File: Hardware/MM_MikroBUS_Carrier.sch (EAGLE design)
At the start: 50 parts, among them J15 MICROMOD-2222-C, J2 QWIIC_RIGHT_ANGLE, J5 Vertical Qwiic Connector, U1 MCP73831, U5 AP7361C-33FGEUDFN-8

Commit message: Working on proto
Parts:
- added U3: MIKROBUS_SMD_BLACK1, mikroBUS_SMD_BLACK:MIKROBUS_SMD_BLACK1
- H5: value STAND-OFF-REFLOW2.5MM_TALL -> STAND-OFF-REFLOW-M2.5_2.5MM_TALL; device SparkFun-Hardware:STAND-OFF-REFLOW2.5MM_TALL -> SparkFun-Hardware:STAND-OFF-REFLOW-M2.5_2.5MM_TALL
- renumbered U5 to U2
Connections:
- removed net D0: J15.D0, J6.4
- removed net D1: J15.D1/CAM_TRIG, J6.5
- new net 5V: U3.+5V
- new net AN_IN: J15.A0, U3.AN
- new net MIK_INT: J15.D0, U3.INT
- new net MIK_RST: J15.D1/CAM_TRIG, U3.RST
- new net PWM: J15.PWM0, U3.PWM
- new net RX: J15.TX1, U3.RX
- new net TX: J15.RX1, U3.TX
- net 3.3V: now also U3.+3.3V
- net GND: now also U3.GND, U3.GND2
- net SCL: now also U3.SCL
- net SDA: now also U3.SDA
- net SPI_!CS!: now also U3.CS
- net SPI_CIPO: now also U3.CIPO
- net SPI_COPI: now also U3.COPI
- net SPI_SCK: now also U3.SCK
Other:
- note added: "MM-MikroBUS-Carrier"
- note added: "MikroBUS Socket"
- note added: "v01"
- note removed: "MM-Qwiic-Carrier-Single"
- note removed: "v10"

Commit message: Finished proto design
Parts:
- removed TP1, TP2: TEST-POINT3X5, SparkFun-Connectors:TEST-POINT3X5
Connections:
- net MIK_INT: now also J6.5
- net MIK_RST: now also J6.4
- net SCL: no longer TP2.1
- net SDA: no longer TP1.1
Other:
- note removed: "Test Points"
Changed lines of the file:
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@@
 <part name="SUPPLY8" library="SparkFun-PowerSymbols" deviceset="VIN" device=""/>
 <part name="SUPPLY9" library="SparkFun-PowerSymbols" deviceset="VIN" device=""/>
-<part name="TP1" library="SparkFun-Connectors" deviceset="TEST-POINT" device="3X5"/>
-<part name="TP2" library="SparkFun-Connectors" deviceset="TEST-POINT" device="3X5"/>
 <part name="J4" library="SparkFun-Connectors" deviceset="CONN_02" device="1X02_NO_SILK"/>
 <part name="GND14" library="SparkFun-PowerSymbols" deviceset="GND" device=""/>
@@
 <wire x1="330.2" y1="132.08" x2="431.8" y2="132.08" width="0.2032" layer="97" style="longdash"/>
 <text x="381" y="182.88" size="2.54" layer="94" font="vector" align="center">Power Source Select</text>
-<text x="381" y="121.92" size="2.54" layer="94" font="vector" align="center">Test Points</text>
 <text x="109.22" y="25.4" size="1.778" layer="97" font="vector">Qwiic bus conservative
 max current: 226mA</text>
@@
 <instance part="SUPPLY9" gate="G$1" x="22.86" y="236.22" smashed="yes">
 <attribute name="VALUE" x="22.86" y="239.014" size="1.778" layer="96" align="bottom-center"/>
-</instance>
-<instance part="TP1" gate="G$1" x="378.46" y="109.22" smashed="yes">
-<attribute name="NAME" x="375.92" y="111.76" size="1.778" layer="95" font="vector"/>
-</instance>
-<instance part="TP2" gate="G$1" x="378.46" y="99.06" smashed="yes">
-<attribute name="NAME" x="375.92" y="101.6" size="1.778" layer="95" font="vector"/>
 </instance>
 <instance part="J4" gate="G$1" x="307.34" y="139.7" smashed="yes" rot="R180">
@@
 <net name="SDA" class="0">
 <segment>
-<pinref part="TP1" gate="G$1" pin="1"/>
-<wire x1="378.46" y1="109.22" x2="375.92" y2="109.22" width="0.1524" layer="91"/>
-<label x="375.92" y="109.22" size="1.27" layer="95" rot="R180" xref="yes"/>
-</segment>
-<segment>
 <pinref part="J5" gate="G$1" pin="3"/>
 <wire x1="121.92" y1="48.26" x2="127" y2="48.26" width="0.1524" layer="91"/>
@@
 </net>
 <net name="SCL" class="0">
-<segment>
-<pinref part="TP2" gate="G$1" pin="1"/>
-<wire x1="378.46" y1="99.06" x2="375.92" y2="99.06" width="0.1524" layer="91"/>
-<label x="375.92" y="99.06" size="1.27" layer="95" rot="R180" xref="yes"/>
-</segment>
 <segment>
 <pinref part="J5" gate="G$1" pin="4"/>
@@
 <label x="86.36" y="208.28" size="1.27" layer="95" xref="yes"/>
 </segment>
+<segment>
+<pinref part="J6" gate="J1" pin="4"/>
+<wire x1="205.74" y1="20.32" x2="210.82" y2="20.32" width="0.1524" layer="91"/>
+<label x="210.82" y="20.32" size="1.27" layer="95" xref="yes"/>
+</segment>
 </net>
 <net name="AN_IN" class="0">
@@
 <label x="86.36" y="210.82" size="1.27" layer="95" xref="yes"/>
 </segment>
-</net>
+<segment>
+<pinref part="J6" gate="J1" pin="5"/>
+<wire x1="205.74" y1="22.86" x2="210.82" y2="22.86" width="0.1524" layer="91"/>
+<label x="210.82" y="22.86" size="1.27" layer="95" xref="yes"/>
+</segment>
+</net>

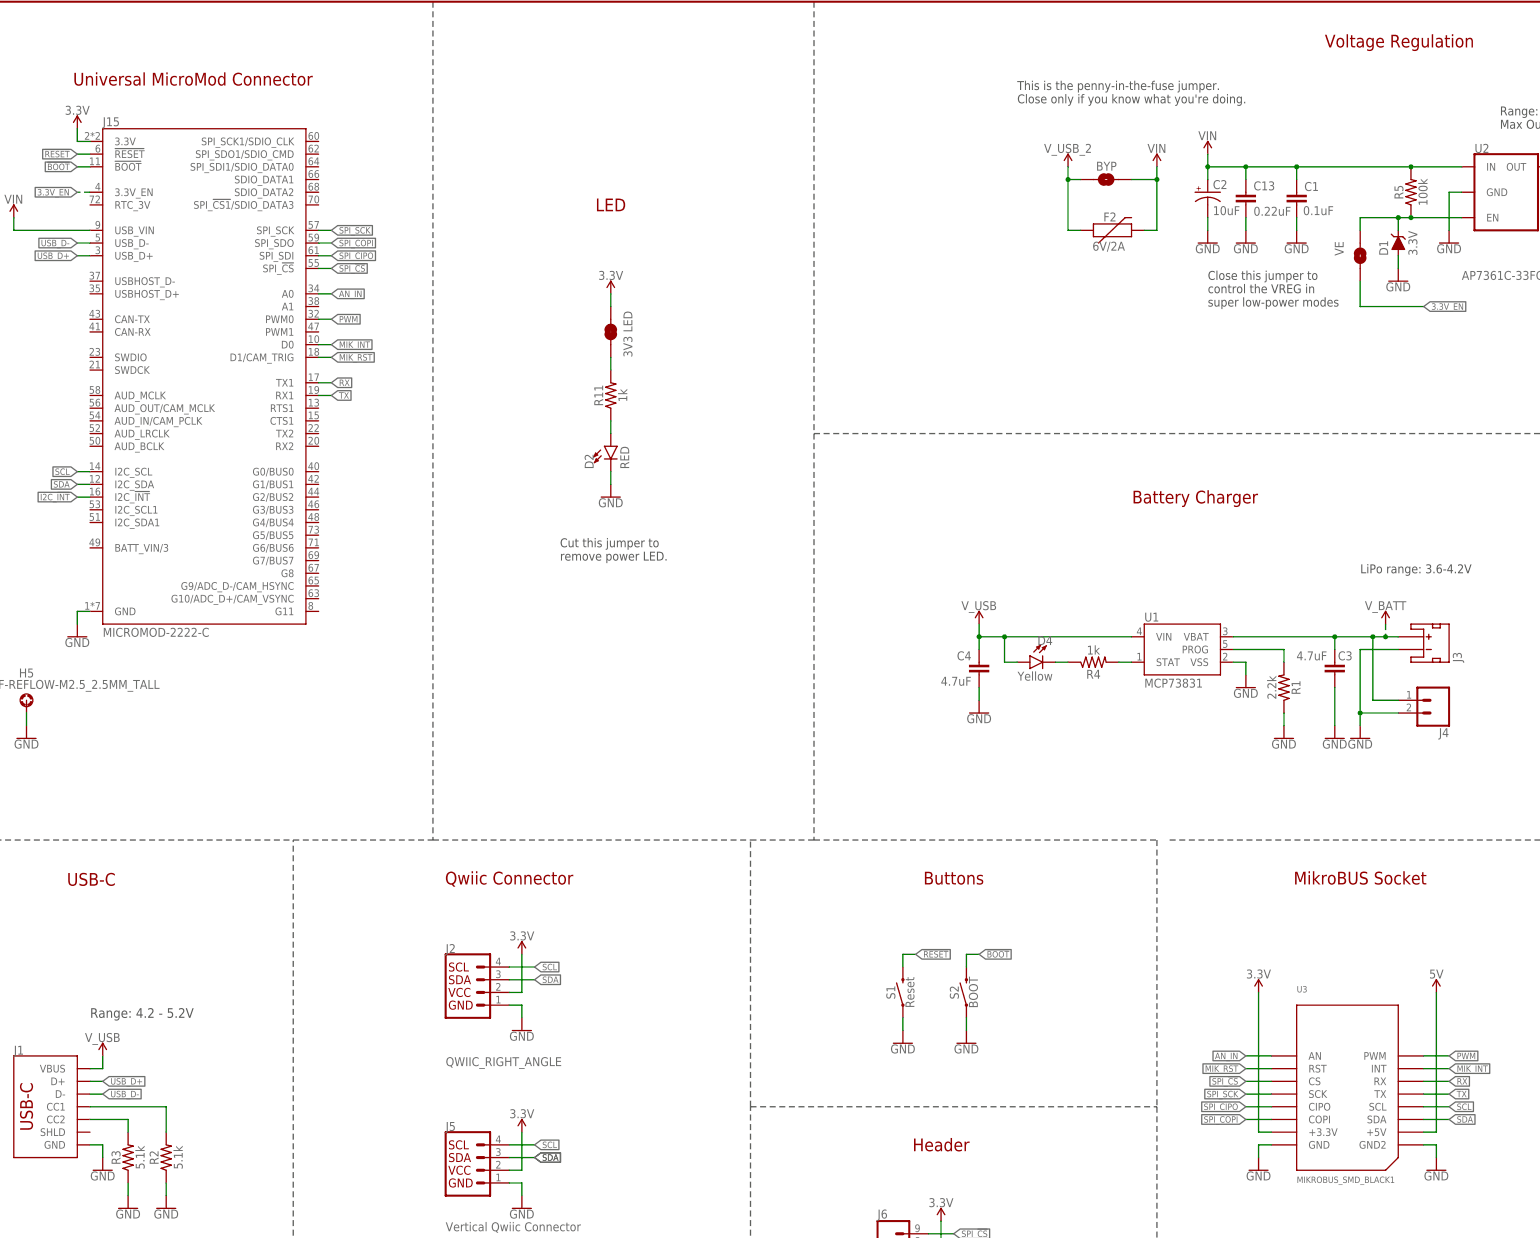
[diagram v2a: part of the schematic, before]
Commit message: Updates from proto design review
MikroBUS device:
* add pin numbers back into sch symbol
* label with a "J" prefix
* Center anchor/origin
* Remove internal pin labels
Schematic:
* 5V pin needs to be connected to "VIN" net
* Change "AN_IN" net label to "AN"
* Add a reset button for the MikroBUS
Board:
* Rotate MikroBUS 90 degrees
* More room for stand offs
* Add more GND vias
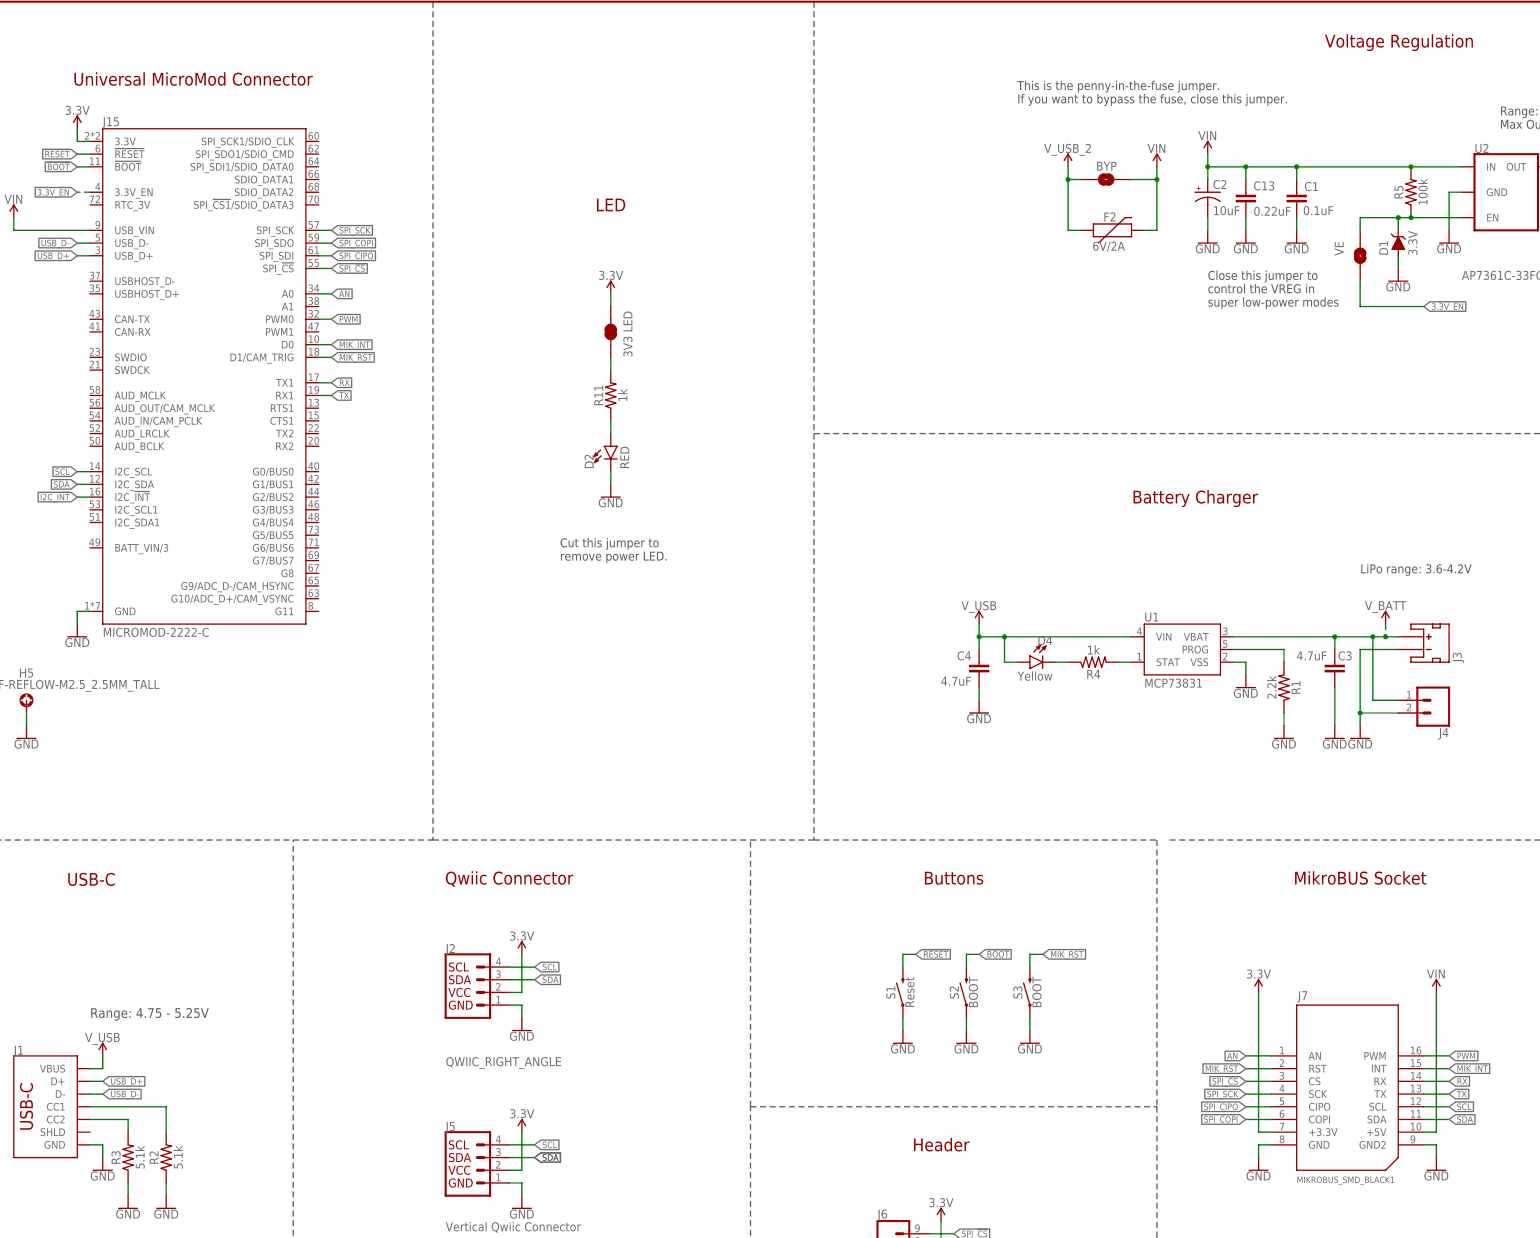
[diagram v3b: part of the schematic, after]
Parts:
- removed U3: MIKROBUS_SMD_BLACK1, mikroBUS_SMD_BLACK:MIKROBUS_SMD_BLACK1
- added J7: MIKROBUS_SMD_BLACK1, mikroBUS_SMD_BLACK:MIKROBUS_SMD_BLACK1
- added S3: BOOT, SparkFun-Switches:MOMENTARY-SWITCH-SPST-SMD-5.2-TALL-REDUNDANT
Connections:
- removed net 5V: U3.+5V
- removed net AN_IN: J15.A0, U3.AN
- new net AN: J15.A0, J7.AN
- net 3.3V: now also J7.+3.3V; no longer U3.+3.3V
- net GND: now also J7.GND, J7.GND2, S3.1; no longer U3.GND, U3.GND2
- net MIK_INT: now also J7.INT; no longer U3.INT
- net MIK_RST: now also J7.RST, S3.2; no longer U3.RST
- net PWM: now also J7.PWM; no longer U3.PWM
- net RX: now also J7.RX; no longer U3.RX
- net SCL: now also J7.SCL; no longer U3.SCL
- net SDA: now also J7.SDA; no longer U3.SDA
- net SPI_!CS!: now also J7.CS; no longer U3.CS
- net SPI_CIPO: now also J7.CIPO; no longer U3.CIPO
- net SPI_COPI: now also J7.COPI; no longer U3.COPI
- net SPI_SCK: now also J7.SCK; no longer U3.SCK
- net TX: now also J7.TX; no longer U3.TX
- net VIN: now also J7.+5V
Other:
- note added: "Range: 4.75 - 5.25V"
- note added: "This is the penny-in-the-fuse jumper. If you want to bypass the fuse, close this jumper."
- note removed: "Range: 4.2 - 5.2V"
- note removed: "This is the penny-in-the-fuse jumper. Close only if you know what you're doing."
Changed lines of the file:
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@@
 <?xml version="1.0" encoding="utf-8"?>
 <!DOCTYPE eagle SYSTEM "eagle.dtd">
-<eagle version="9.4.2">
+<eagle version="9.5.2">
 <drawing>
 <settings>
-<setting alwaysvectorfont="yes"/>
+<setting alwaysvectorfont="no"/>
 <setting verticaltext="up"/>
 </settings>
@@
 <part name="J6" library="SparkFun-Connectors" deviceset="CONN_09" device="NO_SILK"/>
 <part name="SUPPLY17" library="SparkFun-PowerSymbols" deviceset="3.3V" device=""/>
-<part name="U3" library="mikroBUS_SMD_BLACK" deviceset="MIKROBUS_SMD_BLACK" device="1" package3d_urn="urn:adsk.eagle:package:18494266/4"/>
+<part name="J7" library="mikroBUS_SMD_BLACK" deviceset="MIKROBUS_SMD_BLACK" device="1" package3d_urn="urn:adsk.eagle:package:18494266/4"/>
 <part name="GND7" library="SparkFun-PowerSymbols" deviceset="GND" device=""/>
 <part name="GND12" library="SparkFun-PowerSymbols" deviceset="GND" device=""/>
 <part name="SUPPLY18" library="SparkFun-PowerSymbols" deviceset="3.3V" device=""/>
-<part name="SUPPLY19" library="SparkFun-PowerSymbols" deviceset="5V" device=""/>
+<part name="SUPPLY19" library="SparkFun-PowerSymbols" deviceset="VIN" device=""/>
+<part name="S3" library="SparkFun-Switches" deviceset="MOMENTARY-SWITCH-SPST" device="-SMD-5.2-TALL-REDUNDANT" value="BOOT"/>
+<part name="GND11" library="SparkFun-PowerSymbols" deviceset="GND" device=""/>
 </parts>
 <sheets>
@@
 <text x="132.08" y="167.64" size="1.778" layer="97" font="vector">Cut this jumper to
 remove power LED.</text>
-<text x="38.1" y="76.2" size="1.9304" layer="97" font="vector">Range: 4.2 - 5.2V</text>
+<text x="38.1" y="76.2" size="1.9304" layer="97" font="vector">Range: 4.75 - 5.25V</text>
 <text x="299.974" y="271.526" size="2.54" layer="94" font="vector" align="center">Voltage Regulation</text>
 <text x="320.04" y="254" size="1.778" layer="97" font="vector">Range: 2.2 - 6.0V
@@
 super low-power modes</text>
 <text x="223.52" y="259.08" size="1.778" layer="97" font="vector">This is the penny-in-the-fuse jumper.
-Close only if you know what you're doing.</text>
+If you want to bypass the fuse, close this jumper.</text>
 <wire x1="0" y1="111.76" x2="78.74" y2="111.76" width="0.2032" layer="97" style="longdash"/>
 <wire x1="78.74" y1="0" x2="78.74" y2="111.76" width="0.2032" layer="97" style="longdash"/>
@@
 <attribute name="VALUE" x="208.28" y="38.354" size="1.778" layer="96" align="bottom-center"/>
 </instance>
-<instance part="U3" gate="U1" x="289.56" y="58.42" smashed="yes">
-<attribute name="NAME" x="279.4" y="81.28" size="1.27" layer="95"/>
+<instance part="J7" gate="J1" x="289.56" y="58.42" smashed="yes">
+<attribute name="NAME" x="279.654" y="79.756" size="1.778" layer="95"/>
 <attribute name="VALUE" x="279.4" y="43.18" size="1.27" layer="96"/>
 </instance>
@@
 <instance part="SUPPLY19" gate="G$1" x="307.34" y="81.28" smashed="yes">
 <attribute name="VALUE" x="307.34" y="84.074" size="1.778" layer="96" align="bottom-center"/>
+</instance>
+<instance part="S3" gate="G$1" x="226.06" y="81.28" smashed="yes" rot="R90">
+<attribute name="NAME" x="224.536" y="81.28" size="1.778" layer="95" font="vector" rot="R90" align="bottom-center"/>
+<attribute name="VALUE" x="226.568" y="81.28" size="1.778" layer="96" font="vector" rot="R90" align="top-center"/>
+</instance>
+<instance part="GND11" gate="1" x="226.06" y="71.12" smashed="yes" rot="MR0">
+<attribute name="VALUE" x="226.06" y="70.866" size="1.778" layer="96" rot="MR0" align="top-center"/>
 </instance>
 </instances>
@@
 </segment>
 <segment>
-<pinref part="U3" gate="U1" pin="GND"/>
+<pinref part="J7" gate="J1" pin="GND"/>
 <wire x1="274.32" y1="50.8" x2="271.78" y2="50.8" width="0.1524" layer="91"/>
 <wire x1="271.78" y1="50.8" x2="271.78" y2="48.26" width="0.1524" layer="91"/>
@@
 </segment>
 <segment>
-<pinref part="U3" gate="U1" pin="GND2"/>
+<pinref part="J7" gate="J1" pin="GND2"/>
 <wire x1="304.8" y1="50.8" x2="307.34" y2="50.8" width="0.1524" layer="91"/>
 <wire x1="307.34" y1="50.8" x2="307.34" y2="48.26" width="0.1524" layer="91"/>
 <pinref part="GND12" gate="1" pin="GND"/>
+</segment>
+<segment>
+<pinref part="S3" gate="G$1" pin="1"/>
+<pinref part="GND11" gate="1" pin="GND"/>
+<wire x1="226.06" y1="73.66" x2="226.06" y2="76.2" width="0.1524" layer="91"/>
 </segment>
 </net>
@@
 </segment>
 <segment>
-<pinref part="U3" gate="U1" pin="+3.3V"/>
+<pinref part="J7" gate="J1" pin="+3.3V"/>
 <wire x1="274.32" y1="53.34" x2="271.78" y2="53.34" width="0.1524" layer="91"/>
 <wire x1="271.78" y1="53.34" x2="271.78" y2="81.28" width="0.1524" layer="91"/>
@@
 <pinref part="SUPPLY10" gate="G$1" pin="VIN"/>
 </segment>
+<segment>
+<pinref part="J7" gate="J1" pin="+5V"/>
+<wire x1="304.8" y1="53.34" x2="307.34" y2="53.34" width="0.1524" layer="91"/>
+<wire x1="307.34" y1="53.34" x2="307.34" y2="81.28" width="0.1524" layer="91"/>
+<pinref part="SUPPLY19" gate="G$1" pin="VIN"/>
+</segment>
 </net>
 <net name="N$1" class="0">
@@
 </segment>
 <segment>
-<pinref part="U3" gate="U1" pin="SDA"/>
+<pinref part="J7" gate="J1" pin="SDA"/>
 <wire x1="304.8" y1="55.88" x2="309.88" y2="55.88" width="0.1524" layer="91"/>
 <label x="309.88" y="55.88" size="1.27" layer="95" xref="yes"/>
@@
 </segment>
 <segment>
-<pinref part="U3" gate="U1" pin="SCL"/>
+<pinref part="J7" gate="J1" pin="SCL"/>
 <wire x1="304.8" y1="58.42" x2="309.88" y2="58.42" width="0.1524" layer="91"/>
 <label x="309.88" y="58.42" size="1.27" layer="95" xref="yes"/>
@@
 </segment>
 <segment>
-<pinref part="U3" gate="U1" pin="SCK"/>
+<pinref part="J7" gate="J1" pin="SCK"/>
 <wire x1="274.32" y1="60.96" x2="269.24" y2="60.96" width="0.1524" layer="91"/>
 <label x="269.24" y="60.96" size="1.27" layer="95" rot="R180" xref="yes"/>
@@
 </segment>
 <segment>
-<pinref part="U3" gate="U1" pin="CS"/>
+<pinref part="J7" gate="J1" pin="CS"/>
 <wire x1="274.32" y1="63.5" x2="269.24" y2="63.5" width="0.1524" layer="91"/>
 <label x="269.24" y="63.5" size="1.27" layer="95" rot="R180" xref="yes"/>
@@
 </segment>
 <segment>
-<pinref part="U3" gate="U1" pin="COPI"/>
+<pinref part="J7" gate="J1" pin="COPI"/>
 <wire x1="274.32" y1="55.88" x2="269.24" y2="55.88" width="0.1524" layer="91"/>
 <label x="269.24" y="55.88" size="1.27" layer="95" rot="R180" xref="yes"/>
@@
 </segment>
 <segment>
-<pinref part="U3" gate="U1" pin="CIPO"/>
+<pinref part="J7" gate="J1" pin="CIPO"/>
 <wire x1="274.32" y1="58.42" x2="269.24" y2="58.42" width="0.1524" layer="91"/>
 <label x="269.24" y="58.42" size="1.27" layer="95" rot="R180" xref="yes"/>
@@
 <net name="MIK_RST" class="0">
 <segment>
-<pinref part="U3" gate="U1" pin="RST"/>
+<pinref part="J7" gate="J1" pin="RST"/>
 <wire x1="274.32" y1="66.04" x2="269.24" y2="66.04" width="0.1524" layer="91"/>
 <label x="269.24" y="66.04" size="1.27" layer="95" rot="R180" xref="yes"/>
@@
 <label x="210.82" y="20.32" size="1.27" layer="95" xref="yes"/>
 </segment>
-</net>
-<net name="AN_IN" class="0">
-<segment>
-<pinref part="U3" gate="U1" pin="AN"/>
+<segment>
+<pinref part="S3" gate="G$1" pin="2"/>
+<wire x1="226.06" y1="86.36" x2="226.06" y2="88.9" width="0.1524" layer="91"/>
+<wire x1="226.06" y1="88.9" x2="228.6" y2="88.9" width="0.1524" layer="91"/>
+<label x="228.6" y="88.9" size="1.27" layer="95" xref="yes"/>
+</segment>
+</net>
+<net name="AN" class="0">
+<segment>
+<pinref part="J7" gate="J1" pin="AN"/>
 <wire x1="274.32" y1="68.58" x2="269.24" y2="68.58" width="0.1524" layer="91"/>
 <label x="269.24" y="68.58" size="1.27" layer="95" rot="R180" xref="yes"/>
@@
 <net name="PWM" class="0">
 <segment>
-<pinref part="U3" gate="U1" pin="PWM"/>
+<pinref part="J7" gate="J1" pin="PWM"/>
 <wire x1="304.8" y1="68.58" x2="309.88" y2="68.58" width="0.1524" layer="91"/>
 <label x="309.88" y="68.58" size="1.27" layer="95" xref="yes"/>
@@
 <net name="MIK_INT" class="0">
 <segment>
-<pinref part="U3" gate="U1" pin="INT"/>
+<pinref part="J7" gate="J1" pin="INT"/>
 <wire x1="304.8" y1="66.04" x2="309.88" y2="66.04" width="0.1524" layer="91"/>
 <label x="309.88" y="66.04" size="1.27" layer="95" xref="yes"/>
@@
 <net name="RX" class="0">
 <segment>
-<pinref part="U3" gate="U1" pin="RX"/>
+<pinref part="J7" gate="J1" pin="RX"/>
 <wire x1="304.8" y1="63.5" x2="309.88" y2="63.5" width="0.1524" layer="91"/>
 <label x="309.88" y="63.5" size="1.27" layer="95" xref="yes"/>
@@
 <net name="TX" class="0">
 <segment>
-<pinref part="U3" gate="U1" pin="TX"/>
+<pinref part="J7" gate="J1" pin="TX"/>
 <wire x1="304.8" y1="60.96" x2="309.88" y2="60.96" width="0.1524" layer="91"/>
 <label x="309.88" y="60.96" size="1.27" layer="95" xref="yes"/>
@@
 </segment>
 </net>
-<net name="5V" class="0">
-<segment>
-<pinref part="U3" gate="U1" pin="+5V"/>
-<wire x1="304.8" y1="53.34" x2="307.34" y2="53.34" width="0.1524" layer="91"/>
-<wire x1="307.34" y1="53.34" x2="307.34" y2="81.28" width="0.1524" layer="91"/>
-<pinref part="SUPPLY19" gate="G$1" pin="5V"/>
-</segment>
-</net>
